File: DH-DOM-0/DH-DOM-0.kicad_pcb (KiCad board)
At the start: 2 copper layers, 40 x 40 mm, 34 parts, among them J1 USB_C_Receptacle_USB2.0_14P, SW1 RST, SW2 BOOT, U1 MMC5983MA, U2 LSM6DSOXTR, U3 ESP32-S3-WROOM-1, U4 NCP1117-3.3_SOT223, U5 TVS1400DRV, U7 ST7789

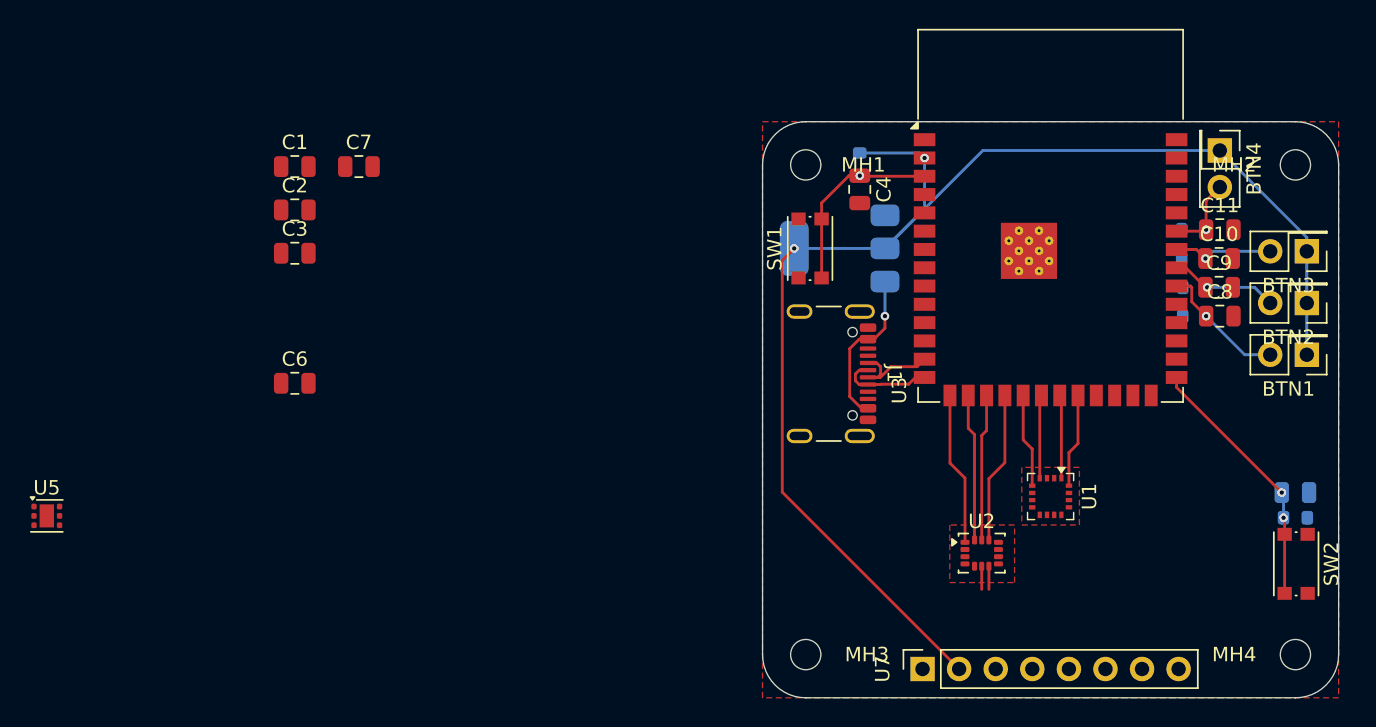
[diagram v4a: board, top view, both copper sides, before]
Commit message: edit
pcb almost done, last decoupling capacitors and screen routing left. also needs drc check
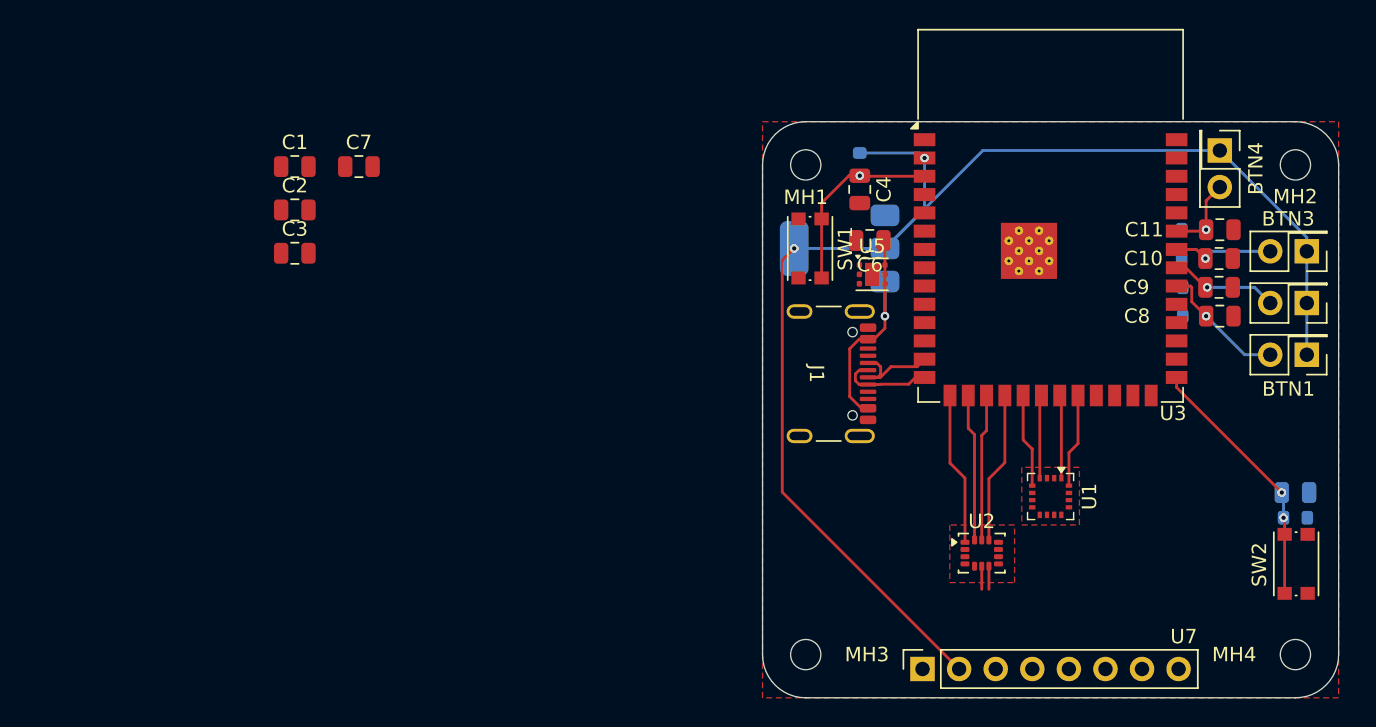
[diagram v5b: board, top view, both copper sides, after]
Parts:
- moved U5 59.7 mm to (178.1, 96.1)
- moved C6 41.1 mm to (177.9, 93.8), turned to 180 degrees
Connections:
- U3 pad 23: unconnected-(U3-IO21-Pad23) -> /SCLK
- U3 pad 24: unconnected-(U3-IO47-Pad24) -> /MOSI
- U3 pad 25: unconnected-(U3-IO48-Pad25) -> /RESET
- U3 pad 26: unconnected-(U3-IO45-Pad26) -> /SS
- U3 pad 8: unconnected-(U3-IO15-Pad8) -> /BACKLIGHT
- U3 pad 9: unconnected-(U3-IO16-Pad9) -> /D/C
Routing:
- net +5V: track 11.2 -> 16.5 mm
